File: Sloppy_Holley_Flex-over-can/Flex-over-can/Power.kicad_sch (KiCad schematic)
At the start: 8 parts, among them U2 L7805ABD2T-TR

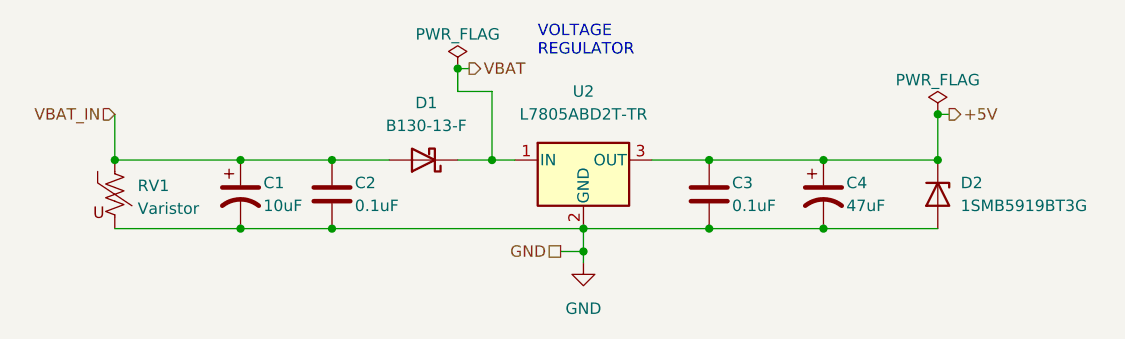
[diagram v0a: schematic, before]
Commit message: Review power/connector sheets, fix ERC, add 3D models for all parts
- Remove duplicate PWR_FLAG on +5V (ERC pin_to_pin error)
- Register KiCad_Footprints and 24pinConnectorSymbol libs for J1
- Correct D1 value to B160-13-F and RV1 to SMDJ24CA to match LCSC parts
- C1: 10uF 50V X5R 1206 (C13585) for load-dump margin
- F2: 0.2A/60V resettable PTC, Brightking SMD1812B020TF-J (C269125)
- Add STEP models for J1, J2 (USB-C), SW1 (BOOT) and fix ESP32 model path
- Project-local footprint copies carry the models for J2, SW1, F2

Co-Authored-By: Claude Opus 5.5 <noreply@anthropic.com>
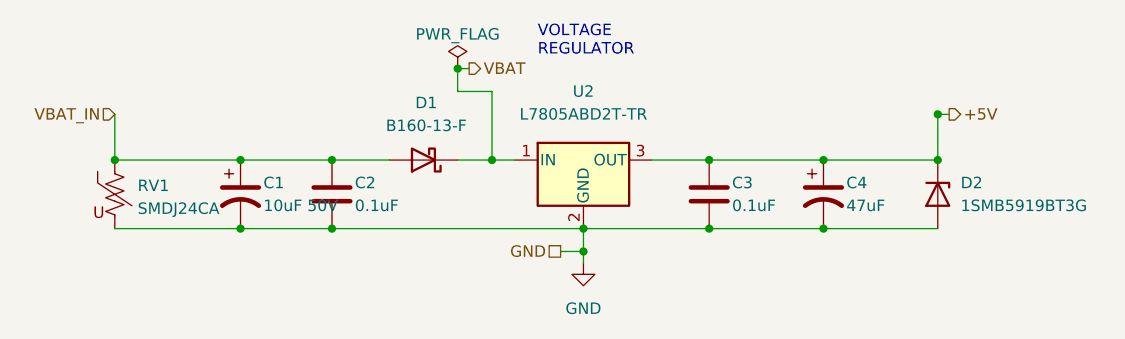
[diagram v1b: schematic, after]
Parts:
- C1: value 10uF -> 10uF 50V; footprint Capacitor_SMD:C_0805_2012Metric -> Capacitor_SMD:C_1206_3216Metric; LCSC C15850 -> C13585; URL https://jlcpcb.com/partdetail/16532-CL21A106KAYNNNE/C15850 -> https://jlcpcb.com/partdetail/14236-CL31A106KBHNNNE/C13585
- D1: value B130-13-F -> B160-13-F
- RV1: value Varistor -> SMDJ24CA
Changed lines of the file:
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@@
 			)
 		)
-		(property "Value" "B130-13-F"
+		(property "Value" "B160-13-F"
 			(at 122.2375 91.44 0)
 			(show_name no)
@@
 			)
 		)
-		(property "Value" "Varistor"
+		(property "Value" "SMDJ24CA"
 			(at 90.17 100.6466 0)
 			(show_name no)
@@
 	)
 	(symbol
-		(lib_id "power:PWR_FLAG")
-		(at 179.07 90.17 0)
-		(unit 1)
-		(body_style 1)
-		(exclude_from_sim no)
-		(in_bom yes)
-		(on_board yes)
-		(in_pos_files yes)
-		(dnp no)
-		(property "Reference" "#FLG02"
-			(at 179.07 88.265 0)
-			(hide yes)
-			(show_name no)
-			(do_not_autoplace no)
-			(effects
-				(font
-					(size 1.27 1.27)
-				)
-			)
-		)
-		(property "Value" "PWR_FLAG"
-			(at 179.07 86.36 0)
-			(show_name no)
-			(do_not_autoplace no)
-			(effects
-				(font
-					(size 1.27 1.27)
-				)
-			)
-		)
-		(property "Footprint" ""
-			(at 179.07 90.17 0)
-			(hide yes)
-			(show_name no)
-			(do_not_autoplace no)
-			(effects
-				(font
-					(size 1.27 1.27)
-				)
-			)
-		)
-		(property "Datasheet" ""
-			(at 179.07 90.17 0)
-			(hide yes)
-			(show_name no)
-			(do_not_autoplace no)
-			(effects
-				(font
-					(size 1.27 1.27)
-				)
-			)
-		)
-		(property "Description" "Special symbol for telling ERC where power comes from"
-			(at 179.07 90.17 0)
-			(hide yes)
-			(show_name no)
-			(do_not_autoplace no)
-			(effects
-				(font
-					(size 1.27 1.27)
-				)
-			)
-		)
-		(pin "1"
-		)
-		(instances
-			(project "Flex-over-can"
-				(path "/52da8c00-1bcc-40cd-af67-a38808218a29/a0c516e1-c011-4b6e-a82e-48eb07b9770c"
-					(reference "#FLG02")
-					(unit 1)
-				)
-			)
-		)
-	)
-	(symbol
 		(lib_id "Device:C_Polarized_US")
 		(at 101.6 99.06 0)
@@
 			)
 		)
-		(property "Value" "10uF"
+		(property "Value" "10uF 50V"
 			(at 104.14 100.33 0)
 			(show_name no)
@@
 			)
 		)
-		(property "Footprint" "Capacitor_SMD:C_0805_2012Metric"
+		(property "Footprint" "Capacitor_SMD:C_1206_3216Metric"
 			(at 101.6 99.06 0)
 			(hide yes)
@@
 			)
 		)
-		(property "Datasheet" "https://jlc-prod-smt.oss-eu-central-1.aliyuncs.com/smtDataManualFile/8579706853607202816-C15850.pdf?response-content-disposition=attachment%3B%20filename%3DC15850.pdf%3B%20filename%2A%3DUTF-8%27%27C15850.pdf&x-oss-date=20260803T143614Z&x-oss-expires=1800&x-oss-security-token=CAISgAN1q6Ft5B2yfSjIr5rcfN6DvJ1s2oCsa0X8plkdZ91ihqLbrzz2IHhMdHJsAOodtv0%2FmmhT6PkclqRLcbhpcmfjV%2BZHzLB8qahm%2FiBV4J7b16cNrbH4M4H6aXeirtuwDsz9SNTCALjPD3nPii50x5bjaDymRCbLGJaViJlhHLN1Ow6jdmhpCctxLAlvo9NgFxm3D%2Fu2NQPwiWf9FVdhvhEG6Vly8qOi2MaRmFy8yFTx0b0SvJ%2BjYMrmPctoN9JnSdC5mfdzau3a1TJ84gRD0a5wkaVA1zbDs5bfISEIuUzebreLqY03dV4mOvdqIcMe8qigz88fk%2FfIioH6xyxKOexoSCnFTOiiupCcQLPyao9jLu6iayqViY7QaIOTqQohZmkAMwVOasAsI3Ngh4zF97Qt0cVNkXO9gWfLI8DtuMleWsrh0tJ%2BqnSgc5lCkRRYwGs1287ugXlSQzo890KPDAEovaKCnZ2ZSfh7Y4sNknI6i%2Bfc2Se2MIkIL%2BFZaaKWD5sagAEY3V6XImRZrsQvHxGZeZbTfAlYmd%2F2lZVI7KFQcbCQXD6WVCvO2YEP4O64CSdK%2BUUJsJSl0ZMXoUfKaVNdGo40qbG2Vsnpbq723fXKLcS9ZJeDl41kfZm4j5WmWb0hPP4MZ5ilBH3hHu5Tw9lstMNihXzh0JAttQMrqcd4cPXPoCAA&x-oss-signature-version=OSS4-HMAC-SHA256&x-oss-credential=STS.NYi7d7QBMmBGicMBYHkRNigpM%2F20260803%2Feu-central-1%2Foss%2Faliyun_v4_request&x-oss-signature=3401558b099106ef6c68a61550fb44e689a3ba3fcd235294cf085a6f46719b79"
+		(property "Datasheet" "https://www.lcsc.com/product-detail/C13585.html"
 			(at 101.6 99.06 0)
 			(hide yes)
@@
 			)
 		)
-		(property "Description" "10uF 25V X5R ±10% 0805 Multilayer Ceramic Capacitors MLCC - SMD/SMT ROHS"
+		(property "Description" "10uF 50V X5R ±10% 1206 MLCC (Samsung CL31A106KBHNNNE)"
 			(at 101.6 99.06 0)
 			(hide yes)
@@
 			)
 		)
-		(property "URL" "https://jlcpcb.com/partdetail/16532-CL21A106KAYNNNE/C15850"
+		(property "URL" "https://jlcpcb.com/partdetail/14236-CL31A106KBHNNNE/C13585"
 			(at 101.6 99.06 0)
 			(hide yes)
@@
 			)
 		)
-		(property "LCSC" "C15850"
+		(property "LCSC" "C13585"
 			(at 101.6 99.06 0)
 			(hide yes)

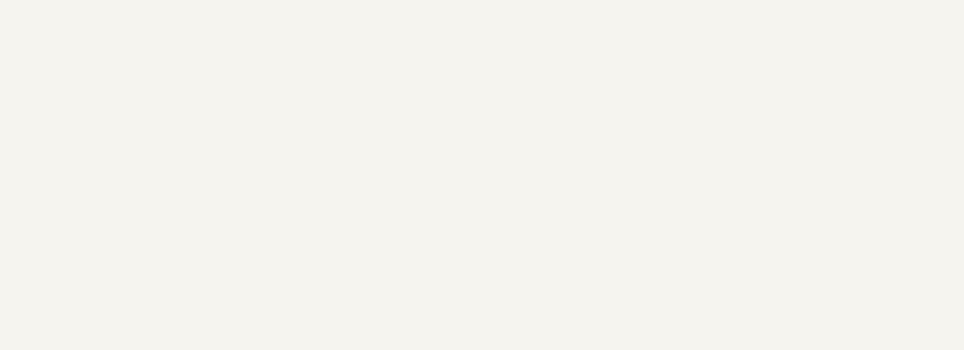
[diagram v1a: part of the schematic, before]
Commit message: Add PCB placement notes for decoupling caps to each sheet
Co-Authored-By: Claude Opus 5.5 <noreply@anthropic.com>
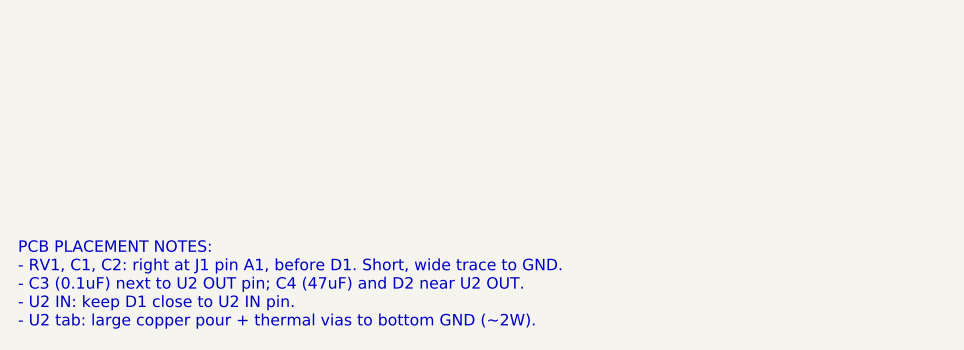
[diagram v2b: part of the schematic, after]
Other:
- note added: "PCB PLACEMENT NOTES: - RV1, C1, C2: right at J1 pin A1, before D1. Short, wide trace to GND. - C3 (0.1uF) next to U2 OUT pin; C4 (47uF) and D2 near U2 OUT. - U2 IN: keep D1 close to U2 IN pin. - U2 tab: large copper pour + thermal vias to bottom GND (~2W)."
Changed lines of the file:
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@@
 		)
 	)
+  (text "PCB PLACEMENT NOTES:\n- RV1, C1, C2: right at J1 pin A1, before D1. Short, wide trace to GND.\n- C3 (0.1uF) next to U2 OUT pin; C4 (47uF) and D2 near U2 OUT.\n- U2 IN: keep D1 close to U2 IN pin.\n- U2 tab: large copper pour + thermal vias to bottom GND (~2W)."
+    (at 15.24 180.34 0)
+    (effects (font (size 1.27 1.27) (color 0 0 194 1)) (justify left bottom))
+  )
 	(symbol
 		(lib_id "Regulator_Linear:L7805")

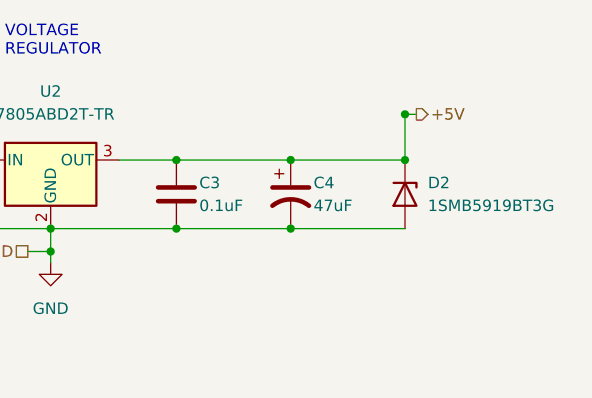
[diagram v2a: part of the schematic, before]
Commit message: Mark R38-R41 (SRP slew resistors) Do-not-populate
R38-R41 only had a "DNP" text field, so BOM and CPL exports would have
placed them. Set the real DNP attribute in the schematic and synced it
to the PCB. KiCad's save also normalized the sheets to LF line endings
and reformatted text notes; no other design changes.

Co-Authored-By: Claude Opus 5.5 <noreply@anthropic.com>
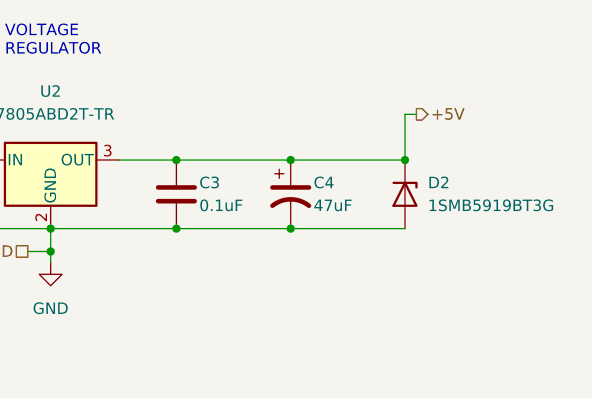
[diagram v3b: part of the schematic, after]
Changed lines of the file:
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@@
 	(generator_version "10.0")
 	(paper "USLetter")
+	(text "PCB PLACEMENT NOTES:\n- RV1, C1, C2: right at J1 pin A1, before D1. Short, wide trace to GND.\n- C3 (0.1uF) next to U2 OUT pin; C4 (47uF) and D2 near U2 OUT.\n- U2 IN: keep D1 close to U2 IN pin.\n- U2 tab: large copper pour + thermal vias to bottom GND (~2W)."
+		(exclude_from_sim no)
+		(at 15.24 180.34 0)
+		(effects
+			(font
+				(size 1.27 1.27)
+				(color 0 0 194 1)
+			)
+			(justify left bottom)
+		)
+	)
 	(text "VOLTAGE\nREGULATOR"
 		(exclude_from_sim no)
@@
 	)
 	(junction
-		(at 179.07 90.17)
-		(diameter 0)
-		(color 0 0 0 0)
-	)
-	(junction
 		(at 153.67 102.87)
 		(diameter 0)
@@
 		)
 	)
-  (text "PCB PLACEMENT NOTES:\n- RV1, C1, C2: right at J1 pin A1, before D1. Short, wide trace to GND.\n- C3 (0.1uF) next to U2 OUT pin; C4 (47uF) and D2 near U2 OUT.\n- U2 IN: keep D1 close to U2 IN pin.\n- U2 tab: large copper pour + thermal vias to bottom GND (~2W)."
-    (at 15.24 180.34 0)
-    (effects (font (size 1.27 1.27) (color 0 0 194 1)) (justify left bottom))
-  )
 	(symbol
 		(lib_id "Regulator_Linear:L7805")
